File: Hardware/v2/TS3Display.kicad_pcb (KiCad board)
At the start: 4 copper layers, 74.1 x 54.9 mm, 26 parts, among them J1 Conn_01x04, J2 Conn_ARM_JTAG_SWD_10, U1 SPX3819M5-L-3-3, U2 USBLC6-2P6, U3 ATSAMD21G18A-AU, U4 NHD-2.8-240320AF-CSXP-F, U5 PAM2804, Y1 32.768k

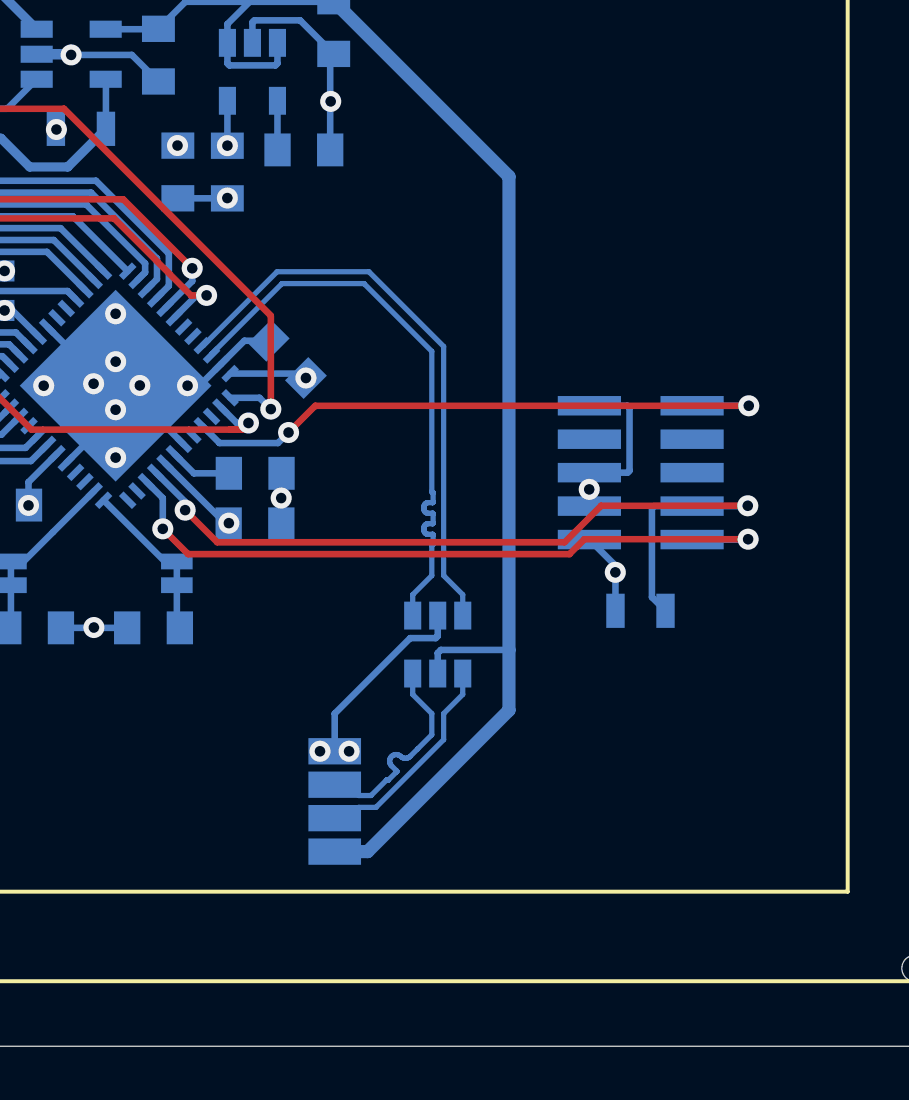
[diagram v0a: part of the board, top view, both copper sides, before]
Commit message: Use different connector for USB connection
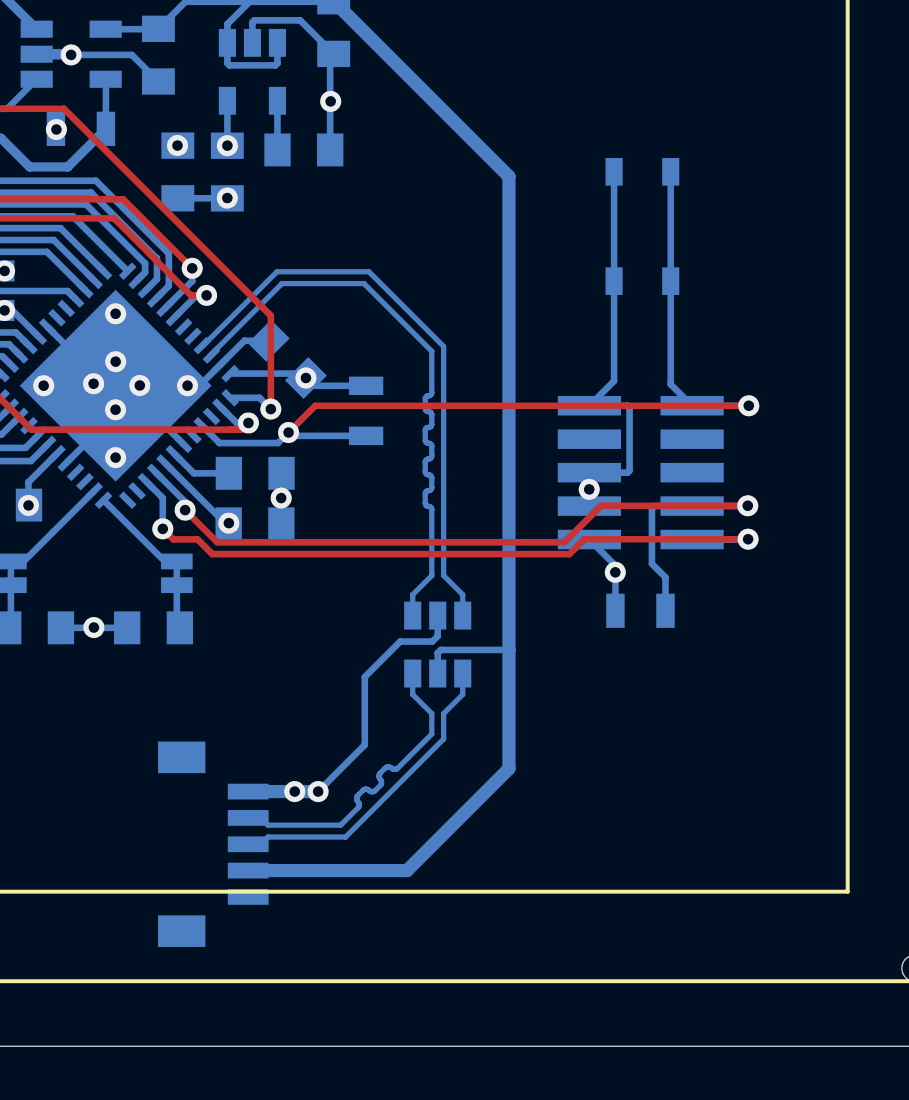
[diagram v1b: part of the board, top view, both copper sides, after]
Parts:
- added R3: 10k, Resistors_SMD:R_0805, B.Cu at (63.0, 43.5)
- added SW1: SW_Push, Buttons_Switches_SMD:SW_SPST_PTS810, B.Cu at (73.5, 36.5)
- J1: value Conn_01x04 -> Conn_01x05; footprint Pin_Headers:Pin_Header_Angled_1x04_Pitch1.27mm -> Connectors_JST:JST_SH_BM05B-SRSS-TB_05x1.00mm_Straight
- moved J1 5.36 mm to (57.3, 60.0), turned to 270 degrees
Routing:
- net GND: track 80.2 -> 93.0 mm
- net ~RESET: track 23.8 -> 36.0 mm
- net 5V: track 56.6 -> 61.5 mm
- net USB_US_D+: track 8.18 -> 11.9 mm
- net USB_US_D-: track 8.18 -> 11.9 mm
- net 3.3V: track 34.7 -> 37.1 mm

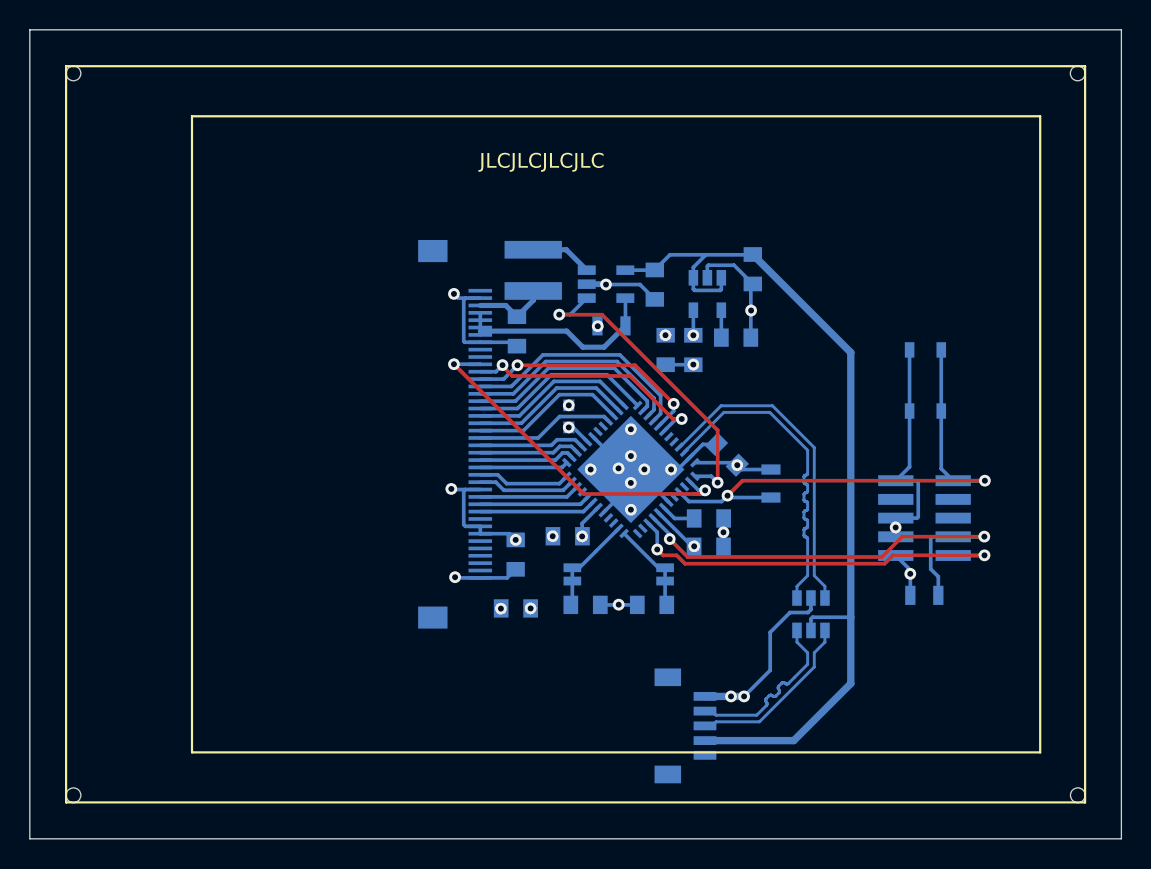
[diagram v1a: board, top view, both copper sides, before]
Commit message: Fix crystal connections
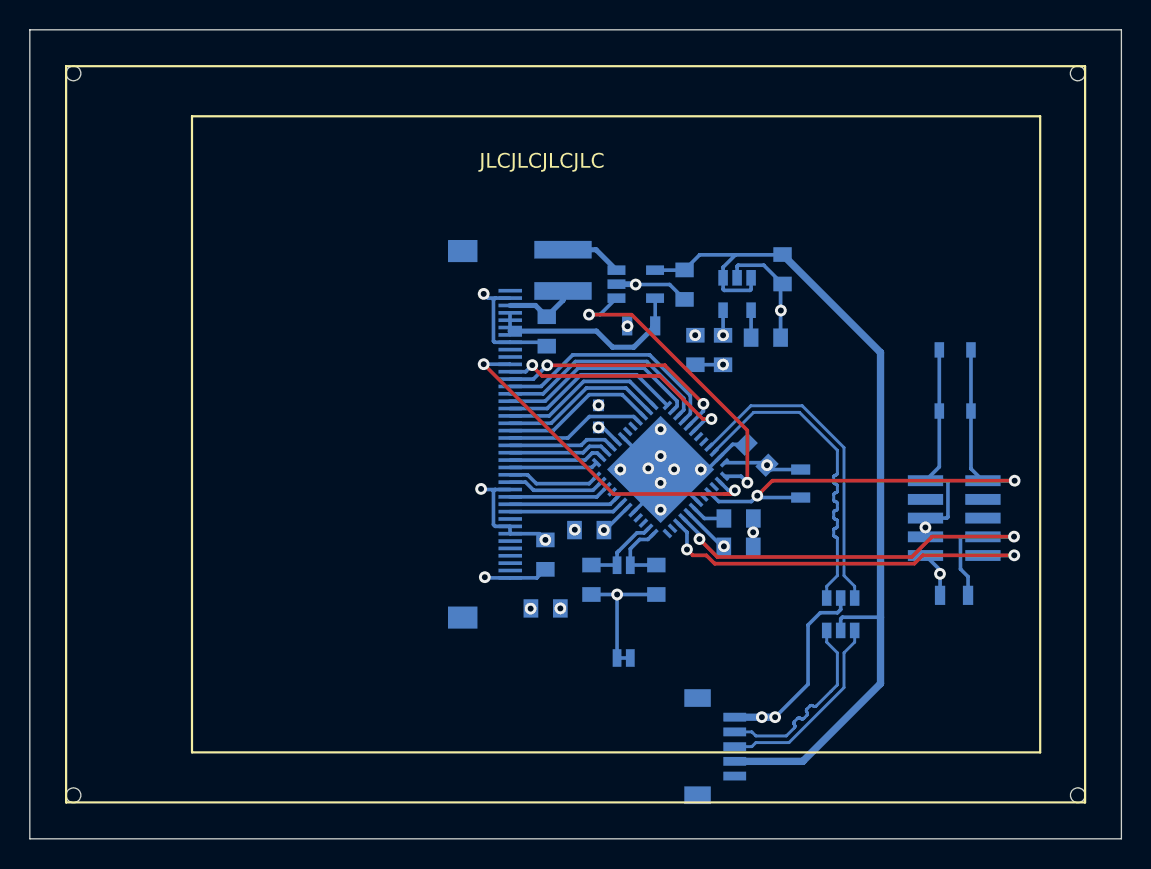
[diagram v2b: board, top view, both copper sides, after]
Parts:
- moved C5 5.10 mm to (55.2, 50.0), turned to 270 degrees
- moved C4 4.46 mm to (50.8, 50.0), turned to 270 degrees
- moved Y1 2.55 mm to (53.0, 52.2), turned to 270 degrees
- moved J1 2.46 mm to (59.3, 61.4)
- moved R3 2.02 mm to (65.0, 43.5)
- moved C1 2.02 mm to (63.8, 29.0)
- moved C10 2.02 mm to (60.8, 47.8)
- moved C11 2.02 mm to (60.8, 45.9)
- moved C12 2.02 mm to (47.7, 52.0)
- moved C13 2.02 mm to (57.2, 30.0)
- moved C14 2.02 mm to (47.7, 48.3)
- moved C15 2.02 mm to (47.8, 33.2)
- moved C2 2.02 mm to (62.7, 33.6)
- moved C3 2.02 mm to (59.8, 34.4)
- moved C7 2.02 mm to (51.3, 39.0)
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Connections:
- U3 pad 1: Net-(C4-Pad1) -> Net-(C5-Pad1)
- U3 pad 2: Net-(C5-Pad1) -> Net-(C4-Pad1)
- Y1 pad 2: Net-(C4-Pad1) -> GND
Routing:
- net GND: track 93.0 -> 101.5 mm
- net Net-(C5-Pad1): track 6.83 -> 4.91 mm
- net USB_US_D-: track 11.9 -> 13.3 mm
- net USB_US_D+: track 11.9 -> 13.2 mm
- net Net-(C4-Pad1): track 6.31 -> 5.61 mm
- net 5V: track 61.5 -> 62.0 mm

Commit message: Fix mirrored LCD FPC pinout
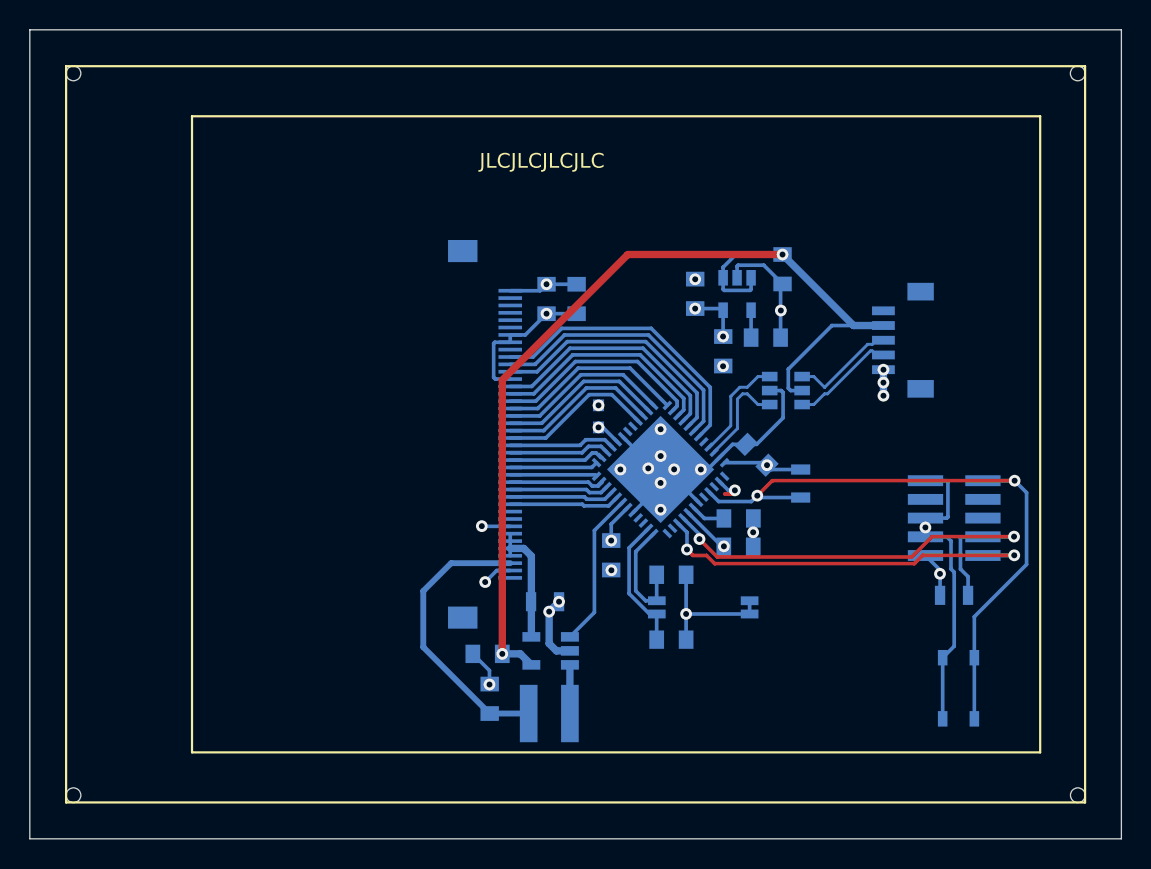
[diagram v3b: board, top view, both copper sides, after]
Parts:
- moved J1 30.3 mm to (71.9, 33.8), turned to 90 degrees
- moved L1 30.1 mm to (48.0, 59.1), turned to 180 degrees
- moved C13 28.4 mm to (43.8, 55.1), turned to 0 degrees
- moved U5 25.6 mm to (48.1, 54.9), turned to 180 degrees
- moved C15 25.2 mm to (43.9, 58.1), turned to 270 degrees
- moved C12 21.1 mm to (49.8, 31.0), turned to 90 degrees
- moved SW1 20.9 mm to (75.8, 57.4)
- moved R1 19.8 mm to (47.7, 51.5), turned to 0 degrees
- moved C14 17.4 mm to (47.8, 31.0), turned to 90 degrees
- moved U2 15.6 mm to (64.0, 37.2), turned to 0 degrees
- moved C4 6.79 mm to (56.3, 54.1), turned to 0 degrees
- moved Y1 5.41 mm to (58.4, 51.9), turned to 0 degrees
- moved C3 4.26 mm to (57.9, 30.6), turned to 90 degrees
- moved C9 2.27 mm to (52.2, 48.4), turned to 270 degrees
- moved C6 1.89 mm to (59.8, 34.5)
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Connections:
- U3 pad 10: ~TFT_WR -> TFT_D14
- U3 pad 11: TFT_D0 -> TFT_D13
- U3 pad 12: TFT_D1 -> TFT_D12
- U3 pad 13: TFT_D2 -> TFT_D11
- U3 pad 14: TFT_D3 -> TFT_D10
- U3 pad 15: TFT_D4 -> TFT_D9
- U3 pad 16: TFT_D5 -> TFT_D8
- U3 pad 21: TFT_D6 -> TFT_D7
- U3 pad 22: TFT_D7 -> TFT_D6
- U3 pad 23: TFT_D8 -> TFT_D5
- U3 pad 24: TFT_D9 -> TFT_D4
- U3 pad 25: TFT_D10 -> TFT_D3
- U3 pad 26: TFT_D11 -> TFT_D2
- U3 pad 27: TFT_D12 -> TFT_D1
- U3 pad 28: TFT_D13 -> TFT_D0
- U3 pad 29: TFT_D14 -> ~TFT_WR
- U3 pad 30: TFT_D15 -> TFT_DC
- U3 pad 31: Net-(U3-Pad31) -> ~TFT_CS
- U3 pad 37: TFT_BL -> Net-(U3-Pad37)
- U3 pad 38: ~TFT_RST -> Net-(U3-Pad38)
- U3 pad 7: ~TFT_CS -> TFT_BL
- U3 pad 8: TFT_DC -> ~TFT_RST
- U3 pad 9: Net-(U3-Pad9) -> TFT_D15
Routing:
- net ~TFT_RST: track 24.6 -> 7.57 mm, vias 2 -> 0
- net USB_D+: track 22.0 -> 6.91 mm
- net USB_D-: track 22.0 -> 7.28 mm
- net LEDA: track 5.01 -> 19.5 mm
- net ~TFT_CS: track 7.91 -> 19.7 mm
- net TFT_DC: track 7.49 -> 18.6 mm
- net TFT_BL: track 21.6 -> 10.6 mm, vias 2 -> 0
- net ~TFT_WR: track 6.87 -> 17.5 mm
- net TFT_D0: track 6.71 -> 16.6 mm
- net TFT_D15: track 17.0 -> 7.20 mm, vias 2 -> 0
- net TFT_D14: track 16.6 -> 6.82 mm, vias 2 -> 0
- net TFT_D13: track 16.2 -> 6.49 mm
- net TFT_D12: track 15.1 -> 5.90 mm
- net TFT_D1: track 6.33 -> 15.5 mm
- net ~RESET: track 36.0 -> 44.7 mm
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
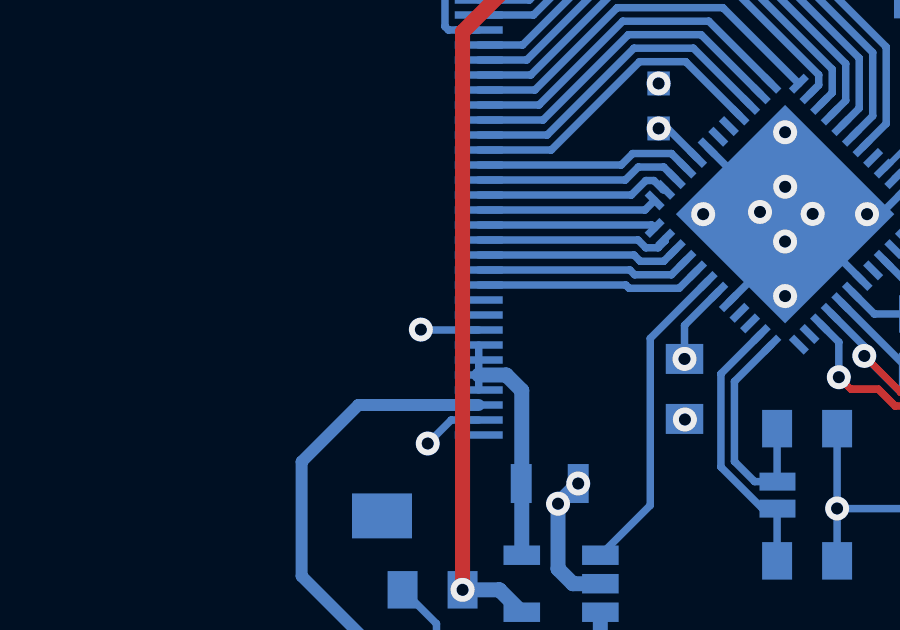
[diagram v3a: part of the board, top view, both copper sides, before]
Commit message: Add missing IM0 pin to display and tie to ground, fixes display not initializing
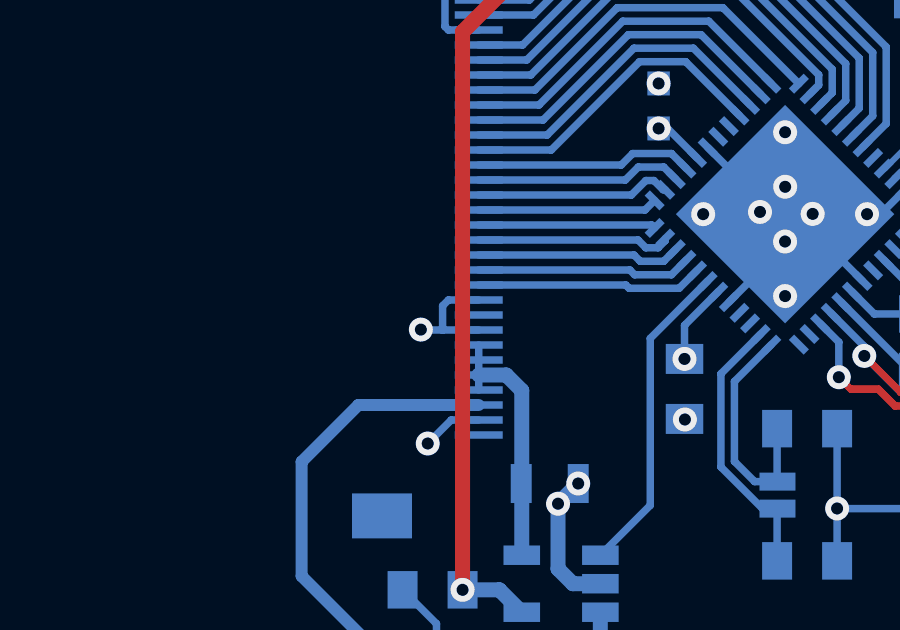
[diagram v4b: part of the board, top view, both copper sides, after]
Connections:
- U4 pad 31: (no net) -> GND
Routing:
- net GND: track 96.9 -> 99.0 mm
